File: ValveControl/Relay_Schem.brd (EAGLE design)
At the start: 101.6 x 53.6 mm, 68 parts, among them Q1 LINEAR_REGULATOR, Q2 LINEAR_REGULATOR, Q3 LINEAR_REGULATOR, Q4 LINEAR_REGULATOR, Q5 LINEAR_REGULATOR

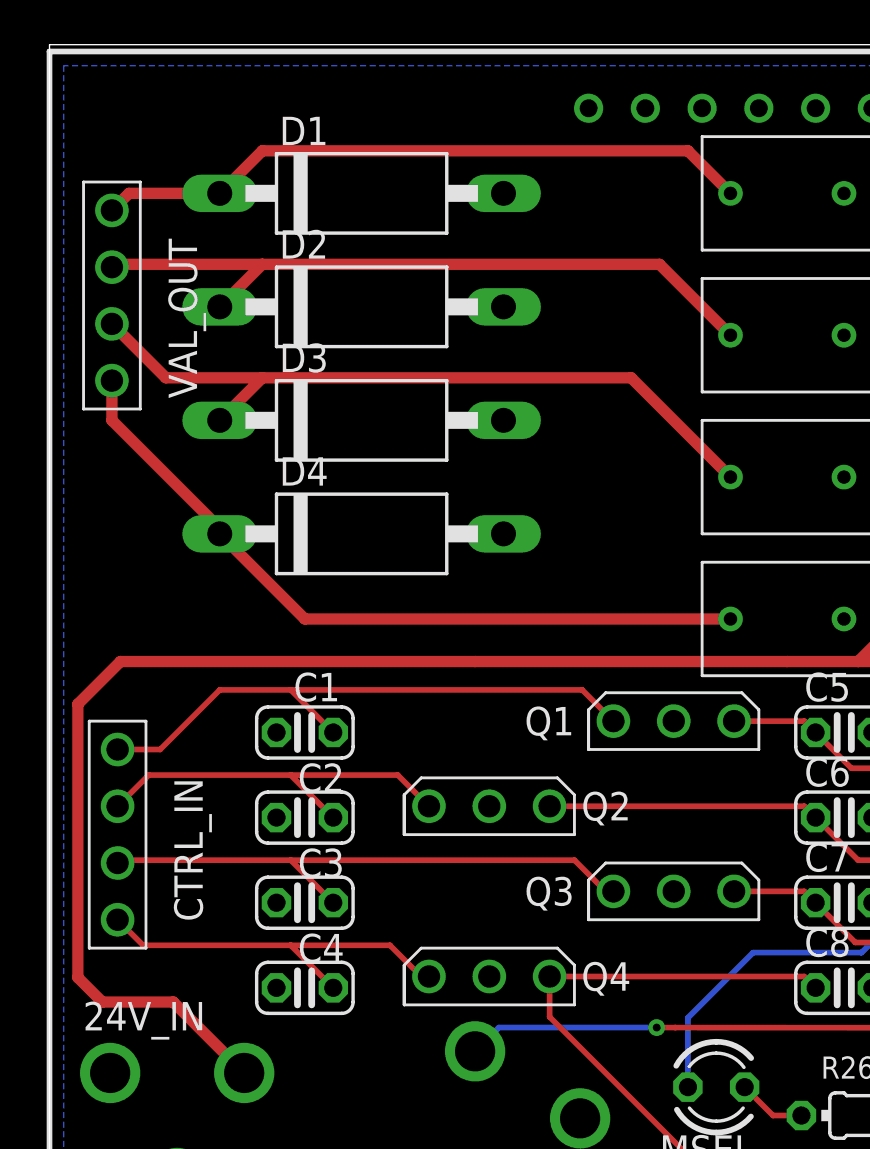
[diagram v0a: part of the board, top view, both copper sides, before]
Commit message: Move some components, add version number to silkscreen
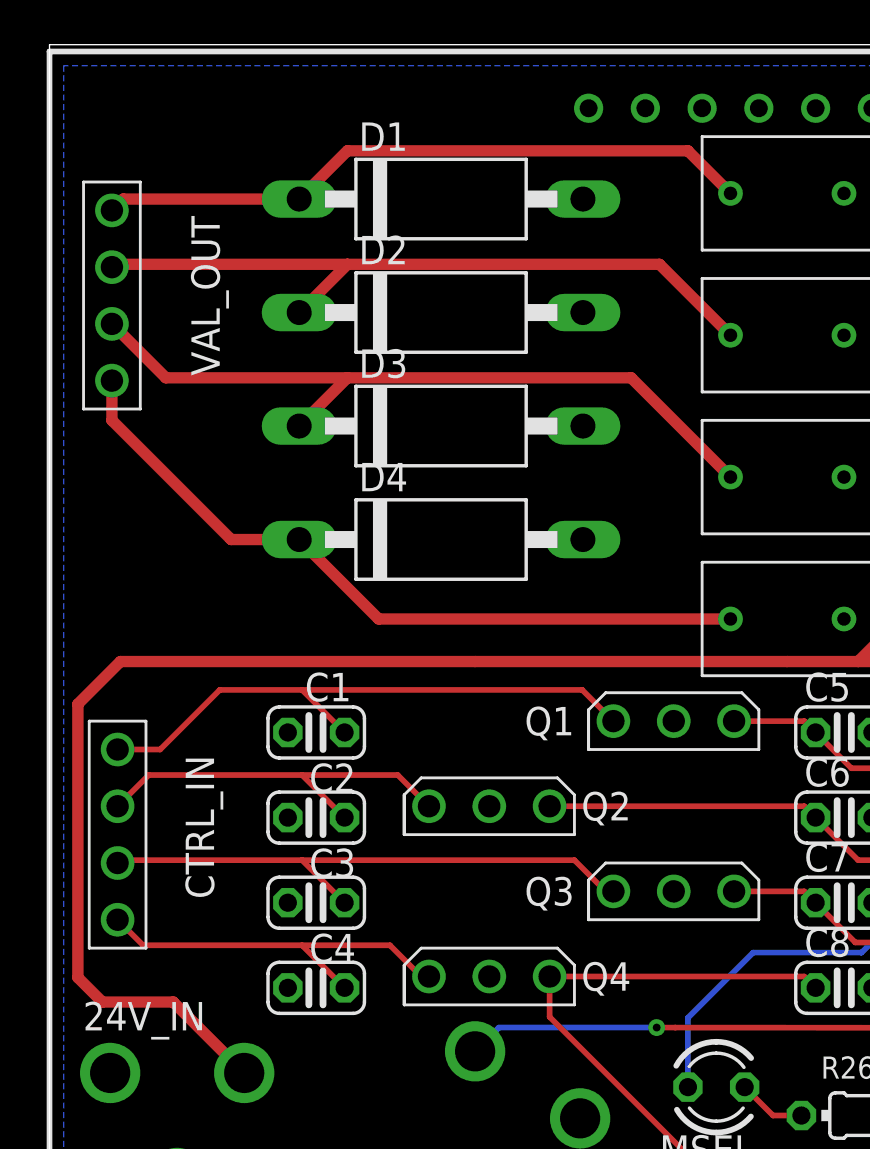
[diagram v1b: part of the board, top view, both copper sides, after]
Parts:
- moved D1 3.57 mm to (17.5, 46.7)
- moved D2 3.57 mm to (17.5, 41.7)
- moved D3 3.57 mm to (17.5, 36.6)
- moved D4 3.57 mm to (17.5, 31.5)
- moved C1 0.51 mm to (11.9, 22.9)
- moved C2 0.51 mm to (11.9, 19.1)
- moved C3 0.51 mm to (11.9, 15.2)
- moved C4 0.51 mm to (11.9, 11.4)
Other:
- board text added: "LPRD Control Board v3.2"
- board text removed: "LPRD Control Board"

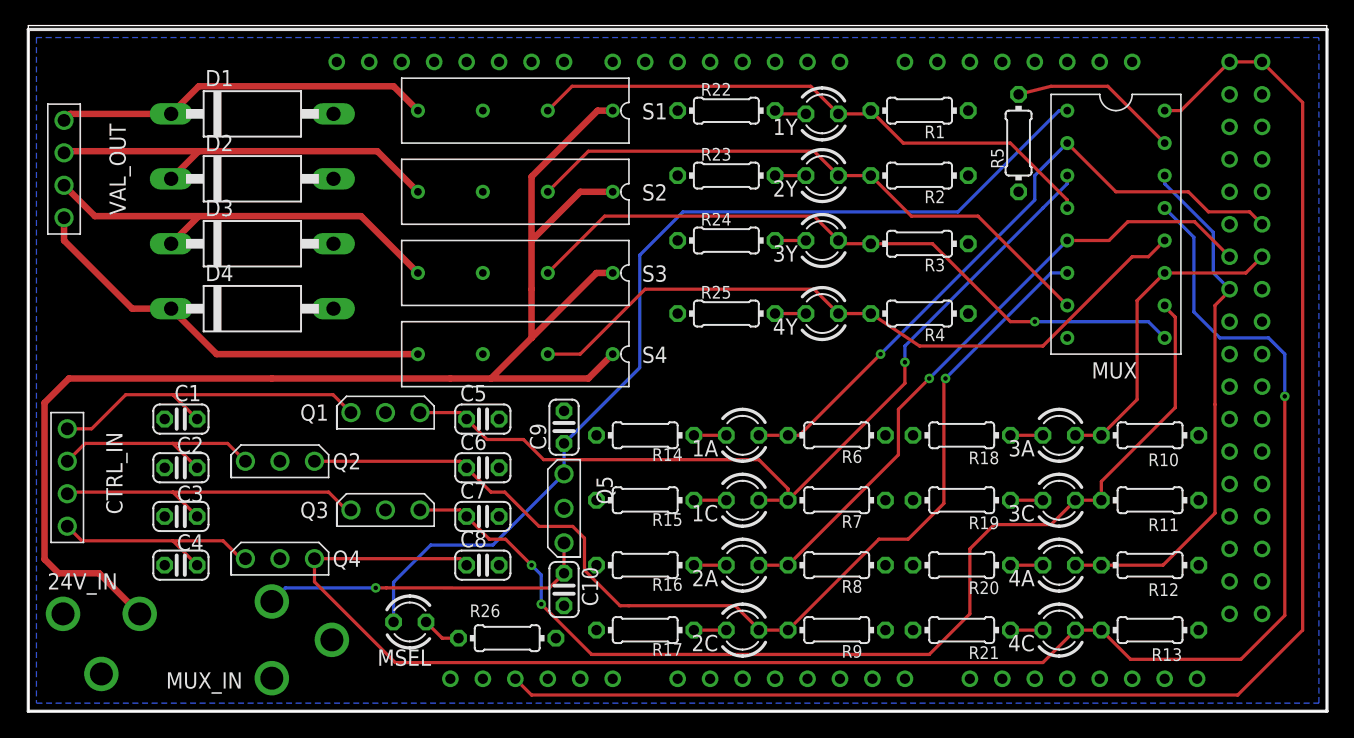
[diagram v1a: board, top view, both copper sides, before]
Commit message: Fix voltage regulators on board
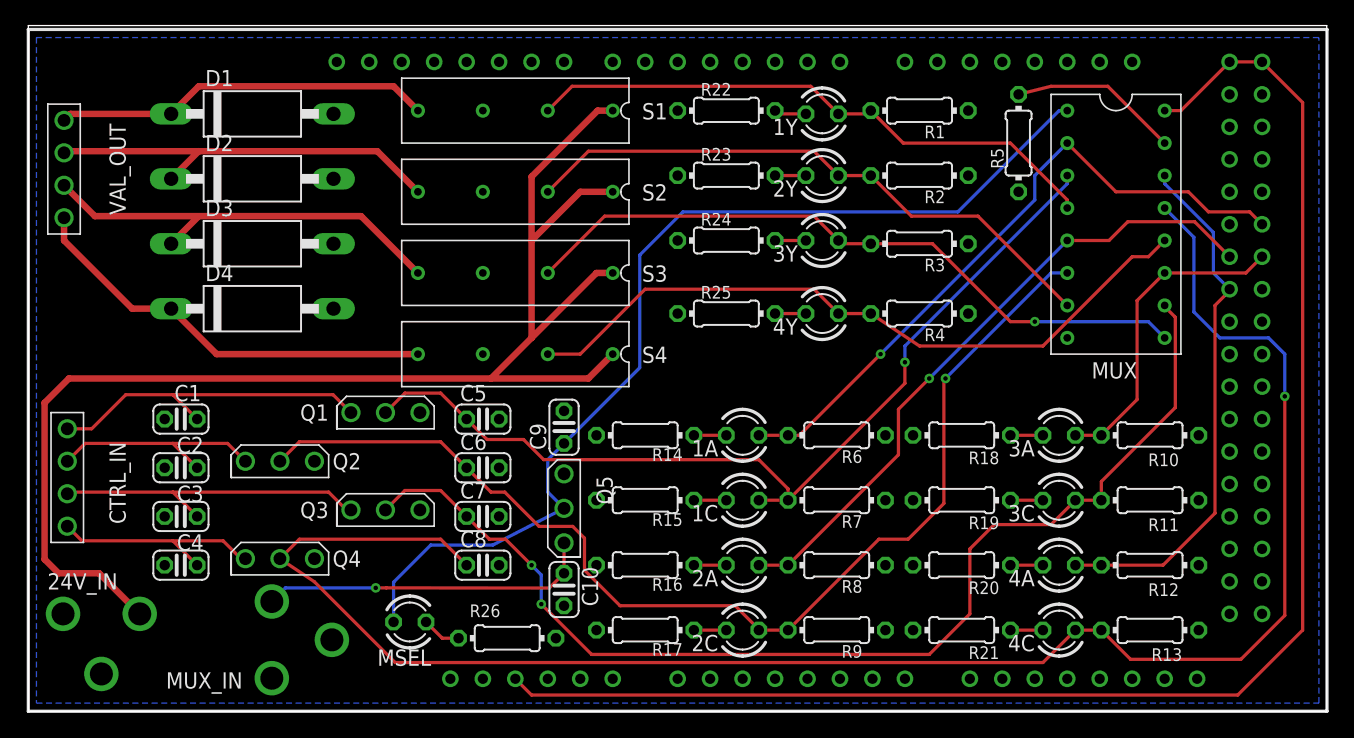
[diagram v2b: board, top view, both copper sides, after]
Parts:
- MUX: device LPRD_RELAY:SN54HC157 -> LPRD_RELAY:SN74HC157
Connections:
- net 0: now also Q1.1, Q2.1, Q3.1, Q4.1, Q5.1; no longer Q1.2, Q2.2, Q3.2, Q4.2, Q5.2
- net 1B: now also Q1.2; no longer Q1.1
- net 2B: now also Q2.2; no longer Q2.1
- net 3B: now also Q3.2; no longer Q3.1
- net 4B: now also Q4.2; no longer Q4.1
- net M_SEL: now also Q5.2; no longer Q5.1
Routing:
- net 4B: track 133.9 -> 139.3 mm
- net 3B: track 85.3 -> 89.2 mm
- net 1B: track 68.9 -> 72.9 mm
- net 2B: track 83.1 -> 87.1 mm
- net M_SEL: track 77.6 -> 79.8 mm
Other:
- board text added: "LPRD Control Board"
- board text removed: "LPRD Control Board v3.2"

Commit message: More fixes/tweaks
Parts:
- 24V_IN: value COAX_POW -> COAX_POW_2.1MM
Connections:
- net 1B: now also Q1.3; no longer Q1.2
- net 2B: now also Q2.3; no longer Q2.2
- net 3B: now also Q3.3; no longer Q3.2
- net 4B: now also Q4.3; no longer Q4.2
- net M_SEL: now also Q5.3; no longer Q5.2
- net N$1: now also Q1.2; no longer Q1.3
- net N$12: now also Q4.2; no longer Q4.3
- net N$2: now also Q2.2; no longer Q2.3
- net N$24: now also Q5.2; no longer Q5.3
- net N$4: now also Q3.2; no longer Q3.3
- net N$6: no longer U$2.5V
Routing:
- net N$6: track 119.2 -> 9.20 mm
- net M_SEL: track 79.8 -> 86.2 mm
- net N$24: track 26.2 -> 29.9 mm
- net N$4: track 25.5 -> 28.0 mm
- net N$1: track 26.6 -> 28.9 mm, vias 0 -> 1
- net 2B: track 87.1 -> 89.4 mm, vias 1 -> 2
- net 4Y: track 55.3 -> 57.6 mm
- net 1B: track 72.9 -> 75.0 mm, vias 1 -> 3
- net 3B: track 89.2 -> 91.4 mm, vias 2 -> 4
- net 4B: track 139.3 -> 141.1 mm, vias 1 -> 2
- net N$12: track 17.7 -> 18.9 mm
- net N$2: track 17.8 -> 18.9 mm
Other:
- board text added: "Glen Smith and Lucas Kramer"
- board text added: "LPRD Control Board v3.2"
- board text removed: "LPRD Control Board"
